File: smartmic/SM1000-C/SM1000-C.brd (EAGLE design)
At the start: 65 x 90 mm, 200 parts, among them CN1 HDR100-3, CN10 MJ-3523-SMT, CN11 HDR100-3, CN12 DF11-16DS, CN2 MOLEX-MINI-B-SMT, CN3 RASM722PX, CN4 RJ-45, CN5 MJ-3523-SMT, CN6 SJ-3524, CN7 MJ-3523-SMT, CN8 SJ-3524, CN9 MJ-3523-SMT, J1 JMP-2PIN, J3 JMP-2PIN, J4 JMP-2PIN, P1 TPAD50, P10 TPAD50, P11 TPAD50, P12 TPAD50, P13 TPAD50, P14 TPAD50, P15 TPAD50, P16 TPAD50, P17 TPAD50, P18 TPAD50, P19 TPAD50, P2 TPAD50, P20 TPAD50, P3 TPAD50, P4 TPAD50, P5 TPAD50, P6 TPAD50, P7 TPAD50, P8 TPAD50, P9 TPAD50, SW1 SW-BOURNS-7914S, SW2 SW-BOURNS-7914S, SW3 DPDT, SW4 SW-BOURNS-7914S, SW5 SW-BOURNS-7914J, T1 SM-LP-5001, T2 SM-LP-5001, U1 STM32F405, U2 LD3985M33R, U3 STMPS2141, U4 EMIF02-USB03F2, U5 TPS54329E, U6 LMV341, U7 LMV341, U8 LM386M-1, U9 LMV341

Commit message: Update Schematic, BOM and add PDFs - RGB
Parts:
- PCB1: value SM1000A -> SM1000C
- moved C64 220.4 mm to (87.5, 69.5)
- moved C65 220.4 mm to (86.5, 64.5)
- moved C66 220.4 mm to (86.5, 61.0)
- moved FB8 220.4 mm to (88.0, 74.0)
- moved C63 198.7 mm to (76.5, 66.0)
- moved C61 192.4 mm to (74.0, 82.0)
- moved R23 192.4 mm to (74.0, 87.0)
- moved R9 192.4 mm to (74.0, 77.0)
- moved R32 143.9 mm to (88.0, 79.5)
- moved CN6 101.8 mm to (13.9, 7.00), flipped to the bottom, turned to 270 degrees
- moved CN8 95.4 mm to (48.0, 7.00), flipped to the bottom, turned to 270 degrees
- moved R22 88.5 mm to (-17.0, 75.5)
- moved C57 88.4 mm to (-11.5, 76.5)
- moved R39 68.3 mm to (-42.0, 76.0)
- moved CN9 64.1 mm to (36.6, 8.00), turned to 270 degrees
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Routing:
- net GND: track 228.0 -> 47.9 mm, vias 46 -> 0
- net !CPPT!: track 77.0 -> 0.00 mm, vias 4 -> 0
- net N$48: track 69.4 -> 0.00 mm, vias 1 -> 0
- net N$65: track 69.2 -> 0.00 mm, vias 2 -> 0
- net MIC: track 68.1 -> 0.00 mm, vias 2 -> 0
- net N$50: track 67.7 -> 0.00 mm, vias 4 -> 0
- net SPKR: track 58.6 -> 0.00 mm, vias 1 -> 0
- net N$63: track 53.1 -> 0.00 mm, vias 1 -> 0
- net N$8: track 51.3 -> 0.00 mm, vias 2 -> 0
- net N$76: track 50.9 -> 0.00 mm, vias 2 -> 0
- net N$9: track 50.9 -> 0.00 mm, vias 1 -> 0
- net OTG_PWR_ON: track 45.8 -> 0.00 mm, vias 4 -> 0
- net APTT: track 44.4 -> 0.00 mm, vias 3 -> 0
- net +5V: track 96.6 -> 53.0 mm, vias 6 -> 0
- net VBUS: track 38.3 -> 0.40 mm, vias 4 -> 0
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- removed copper zone on layer 1, net N$77
- removed copper zone on layer 1, net RF
- removed copper zone on layer 16, net RF
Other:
- board size 65 x 90 mm -> 65 x 100 mm
- board text added: "SM1000 Rev C"
- board text removed: "SM1000 Rev B1"

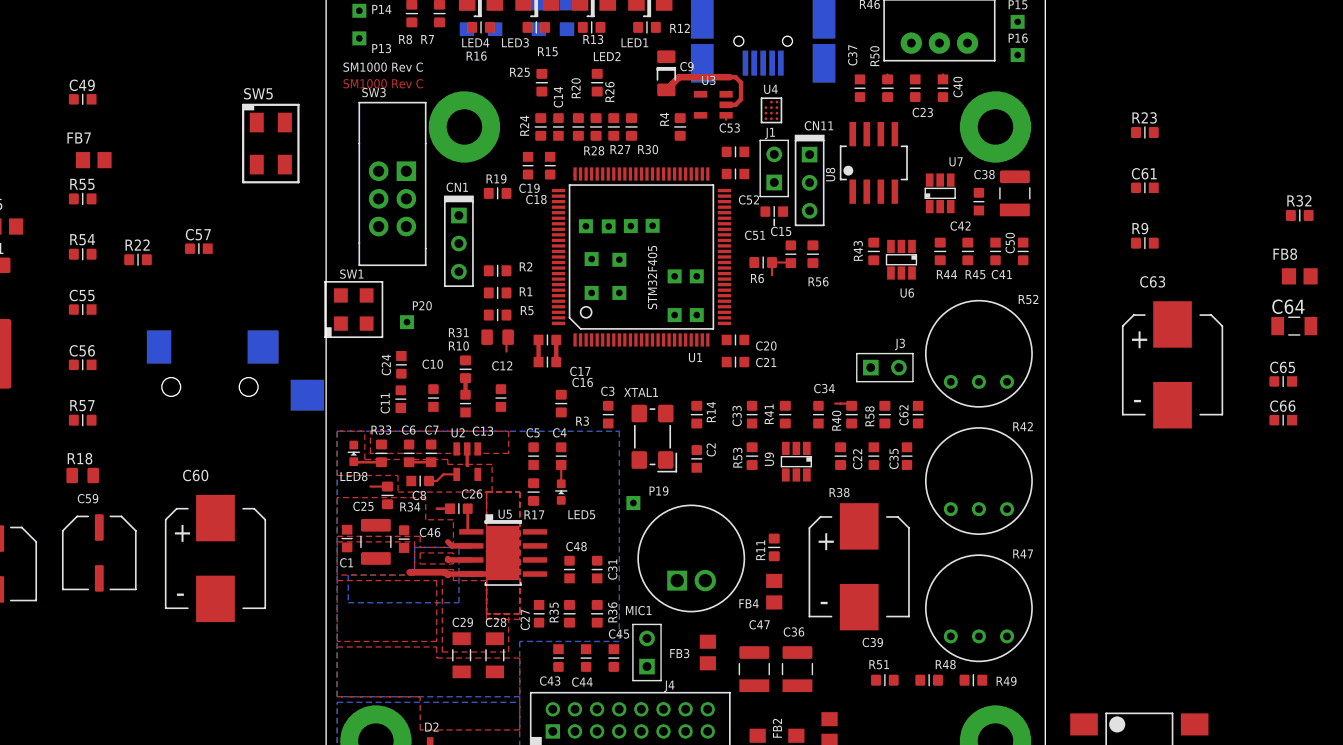
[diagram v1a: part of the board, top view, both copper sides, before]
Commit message: Correct Schematic Part Values RGB
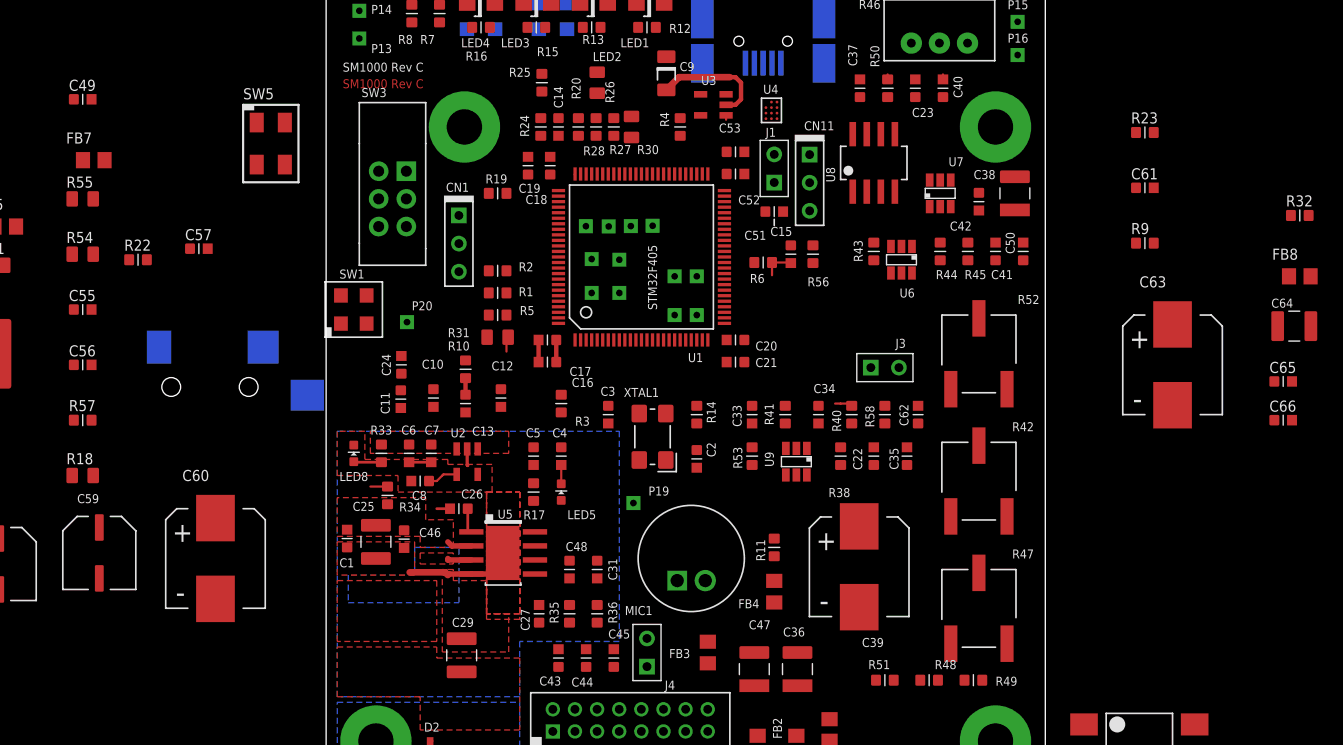
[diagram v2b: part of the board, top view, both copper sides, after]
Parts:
- removed C28: 10uF,25V,1206, ipc-7351-capacitor:CAPC3215X168N
- added SPKR1: SPKR, _RoweTel:NOPACKAGE
- C29, C64: value 10uF,25V,1206 -> 22uF,25V,1210; device ipc-7351-capacitor:CAPC3215X168N -> AA-ipc-7351-capacitor:CAPC3225X168N
- C55, C56: value 1nF,16V -> 1nF,25V
- R26, R30, R54, R55: device AA-ipc-7351-resistor:RESC1608X55N -> AA-ipc-7351-resistor:RESC2012X70N
- R42: value 500K -> 500K,POT; device _RoweTel:TRIMPOT91 -> _RoweTel:POT3361
- R46: value 100K -> 100K,POT
- R47: value 500 -> 500,POT; device _RoweTel:TRIMPOT91 -> _RoweTel:POT3361
- R52: value 1K -> 1K,POT; device _RoweTel:TRIMPOT91 -> _RoweTel:POT3361
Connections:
- removed net N$70: C63.1, R21.1, SW3.3, SW3.6
- new net N$36: C1.2, C25.1, C46.1, C70.1, R21.2, R34.1, U5.2
- net +5V: no longer C28.1
- net +VIN: now also C63.1, R21.1, SW3.3, SW3.6; no longer C1.2, C25.1, C46.1, C70.1, R21.2, R34.1, U5.2
- net GND: no longer C28.2
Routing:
- net N$36: track 0.00 -> 2.28 mm
- net +VIN: track 2.28 -> 0.00 mm

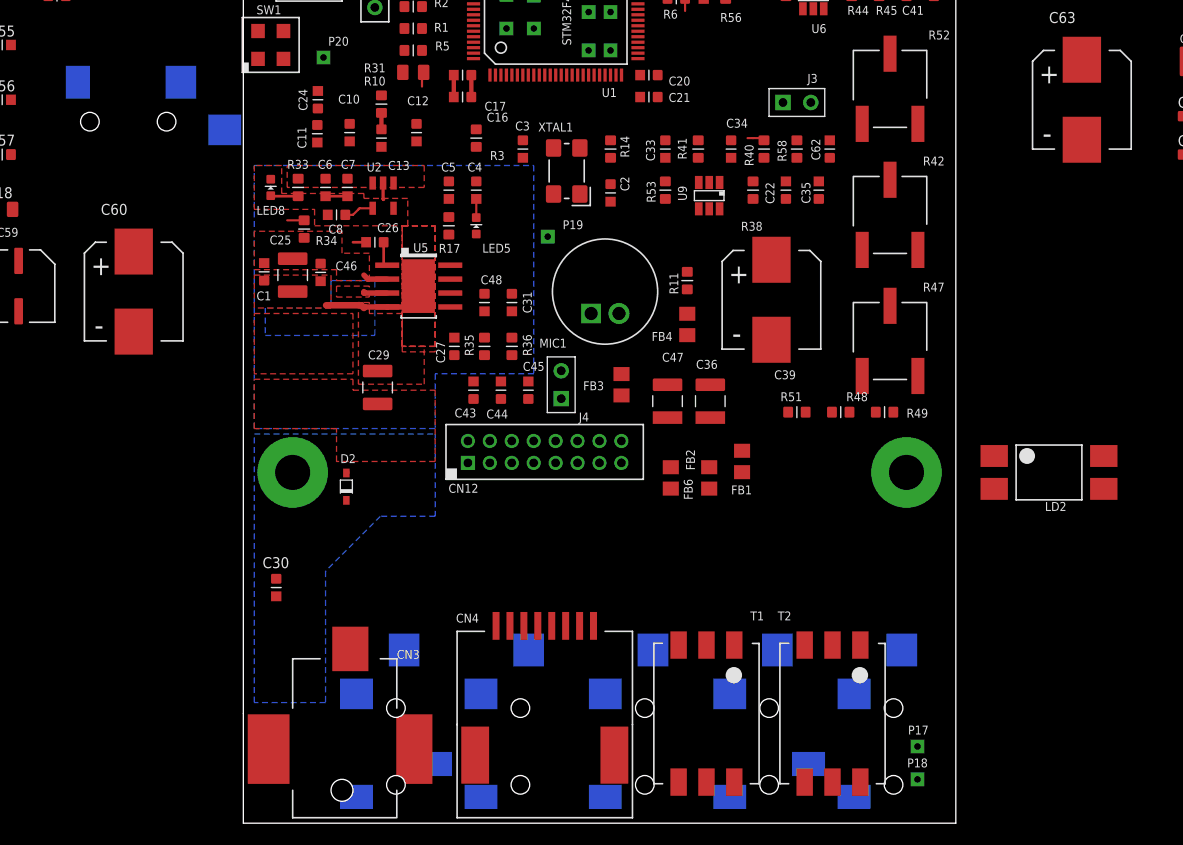
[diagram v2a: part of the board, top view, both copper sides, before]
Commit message: Update Schemaatic, PCB & BOM to reflect change to 0402 package, Change 3.5mm conns to ST-3509 type RGB
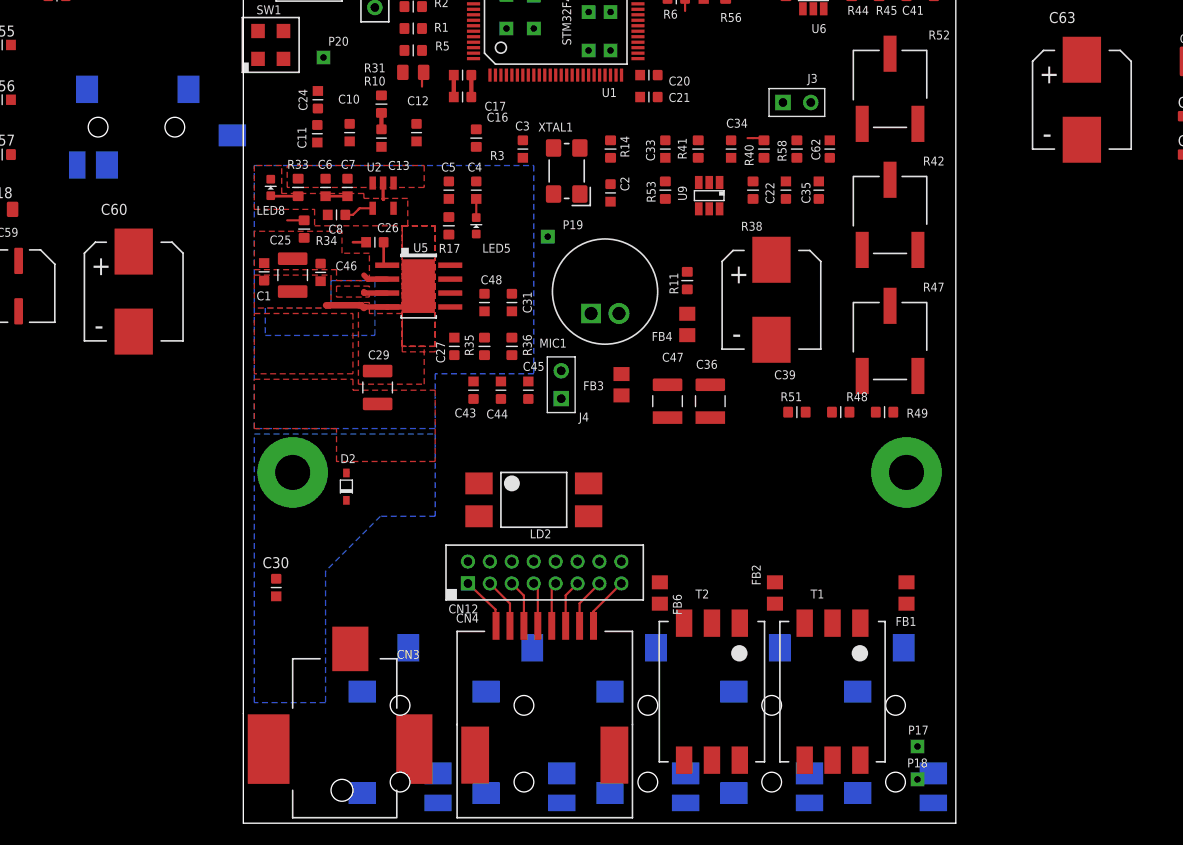
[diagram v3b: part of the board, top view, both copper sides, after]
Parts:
- CN10, CN5, CN7, CN9: value MJ-3523-SMT -> ST-3509; device _RoweTel:MJ-3523-SMT -> _RoweTel:ST-3509
- CN6, CN8: value SJ-3524 -> ST-3509; device _RoweTel:SJ-3524-SMT -> _RoweTel:ST-3509
- moved LD2 47.1 mm to (26.5, 29.5)
- moved CN6 45.6 mm to (59.5, 7.50)
- moved CN5 45.0 mm to (14.3, 7.50)
- moved CN7 22.9 mm to (48.2, 7.50)
- moved CN8 22.4 mm to (25.6, 7.50)
- moved FB1 19.2 mm to (60.5, 21.0)
- moved FB2 12.1 mm to (48.5, 21.0)
- moved T1 11.7 mm to (53.8, 12.0)
- moved T2 11.2 mm to (42.8, 12.0)
- moved CN12 11.0 mm to (27.5, 22.9)
- moved FB6 10.5 mm to (38.0, 21.0)
- moved CN9 0.57 mm to (36.9, 7.50)
- moved CN10 0.50 mm to (-9.50, 63.5)
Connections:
- removed net N$72: CN7.2, FB2.2
- new net N$70: CN7.C, FB2.2
- net APTT: now also CN9.D; no longer CN9.10
- net GND: now also CN5.A, CN8.A; no longer CN10.1, CN5.1, CN8.1
- net MIC: now also CN7.D; no longer CN7.10
- net N$15: now also CN10.C; no longer CN10.2
- net N$60: now also CN5.D; no longer CN5.10
- net N$62: now also CN8.D; no longer CN8.4
- net N$64: now also CN6.C; no longer CN6.2
- net N$73: now also CN9.C; no longer CN9.2
- net N$75: now also CN8.C; no longer CN8.2, CN8.3
- net N$76: now also CN5.C; no longer CN5.2
- net RF_MIC: now also CN7.A; no longer CN7.1
- net RF_PTT: now also CN9.A; no longer CN9.1
- net RF_SPKR: now also CN6.A; no longer CN6.1
- net SPKR: now also CN6.D; no longer CN6.4
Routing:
- net N$58: track 0.00 -> 4.95 mm
- net N$51: track 0.00 -> 4.92 mm
- net N$57: track 0.00 -> 4.63 mm
- net N$52: track 0.00 -> 4.62 mm
- net N$56: track 0.00 -> 4.33 mm
- net N$53: track 0.00 -> 4.32 mm
- net N$55: track 0.00 -> 4.03 mm
- net N$54: track 0.00 -> 4.02 mm

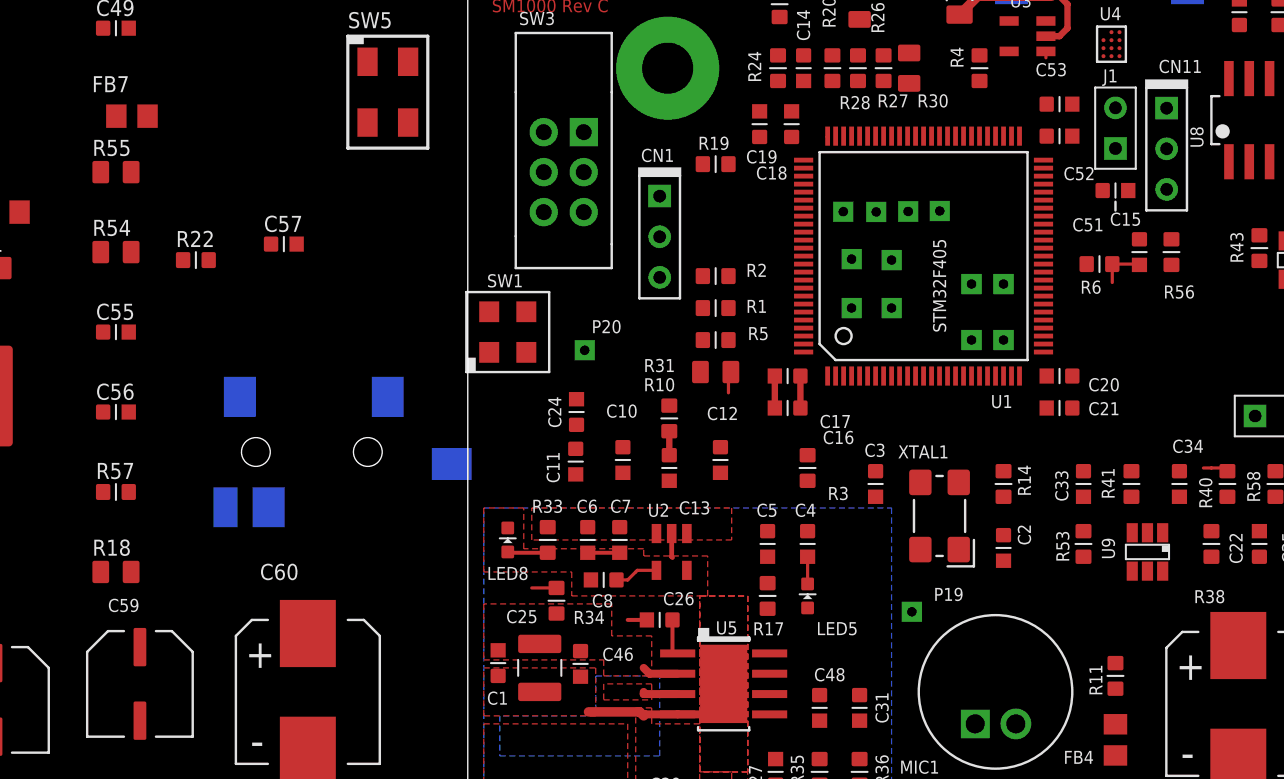
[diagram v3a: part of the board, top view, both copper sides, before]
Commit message: Update schematics, PCB & BOM for addition of 0402 part footprints - RGB
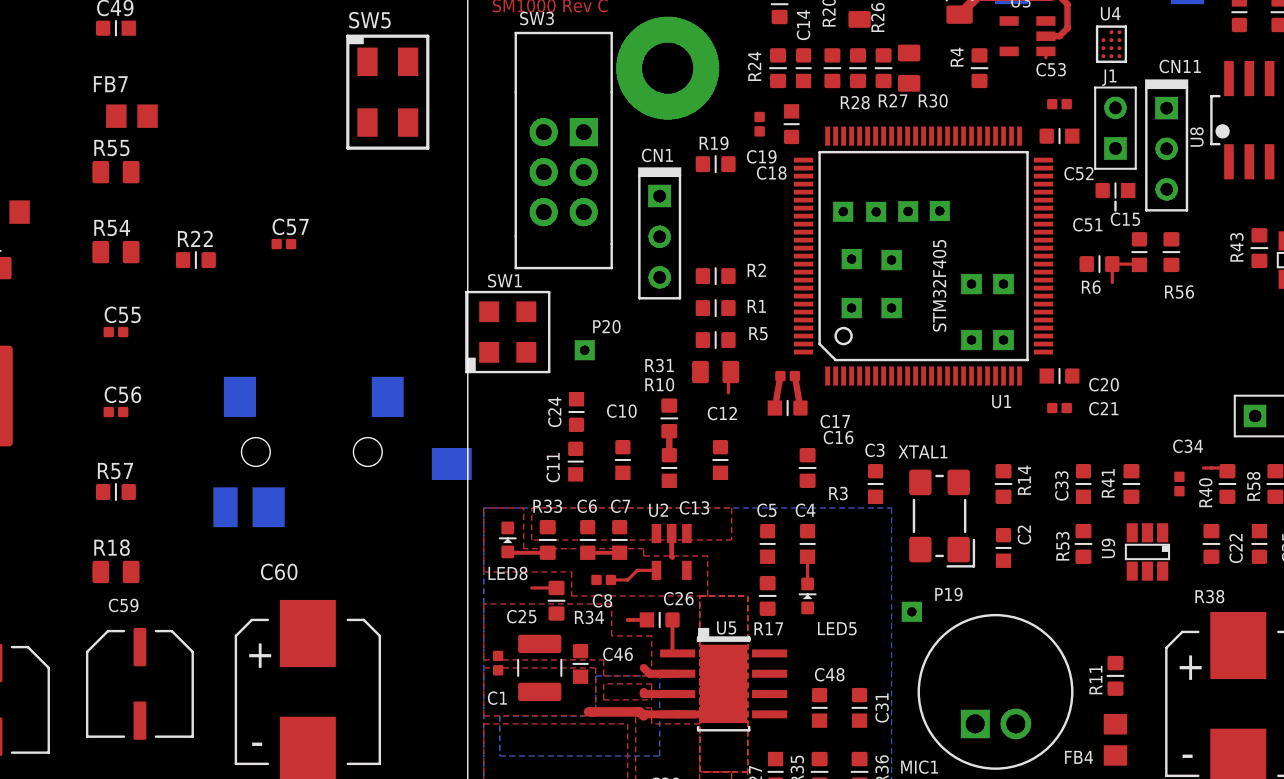
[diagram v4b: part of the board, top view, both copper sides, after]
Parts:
- C1, C34, C55, C56: value 1nF,25V -> 1nF,25V,0402; device AA-ipc-7351-capacitor:CAPC1608X92N -> AA-ipc-7351-capacitor:CAPC1005X60N
- C17, C19, C21, C53, C8: value 10nF,16V -> 10nF,16V,0402; device AA-ipc-7351-capacitor:CAPC1608X92N -> AA-ipc-7351-capacitor:CAPC1005X60N
- C57: value 3.9nF,16V -> 3.9nF,16V,0402; device AA-ipc-7351-capacitor:CAPC1608X92N -> AA-ipc-7351-capacitor:CAPC1005X60N
